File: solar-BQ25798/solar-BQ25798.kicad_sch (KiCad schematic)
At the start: 82 parts, among them J101 Power In, J102 Power OUT, J103 Power OUT, Q101 DMP4013LFGQ-13, Q102 2N7002, U101 HT75xx-1-SOT89, U102 INA219AxDCN

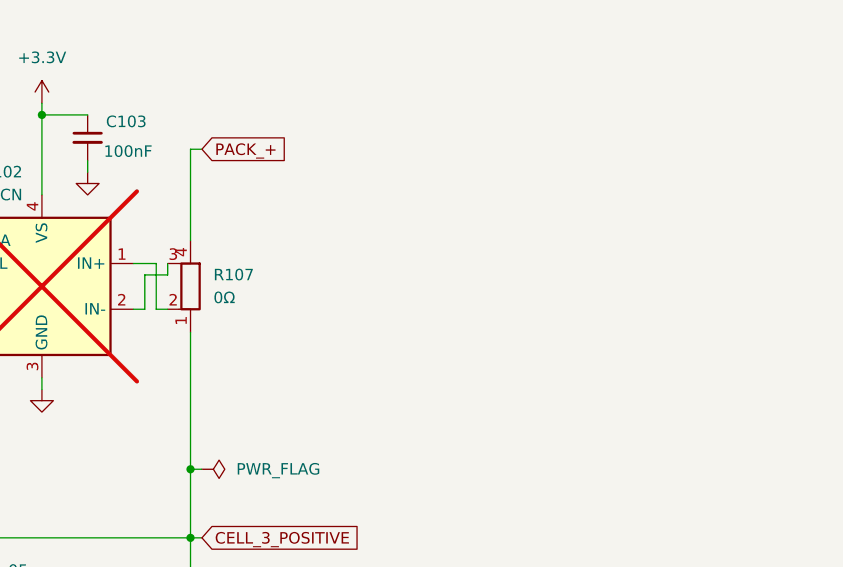
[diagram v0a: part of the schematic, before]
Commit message: Improve optional shunt resistor
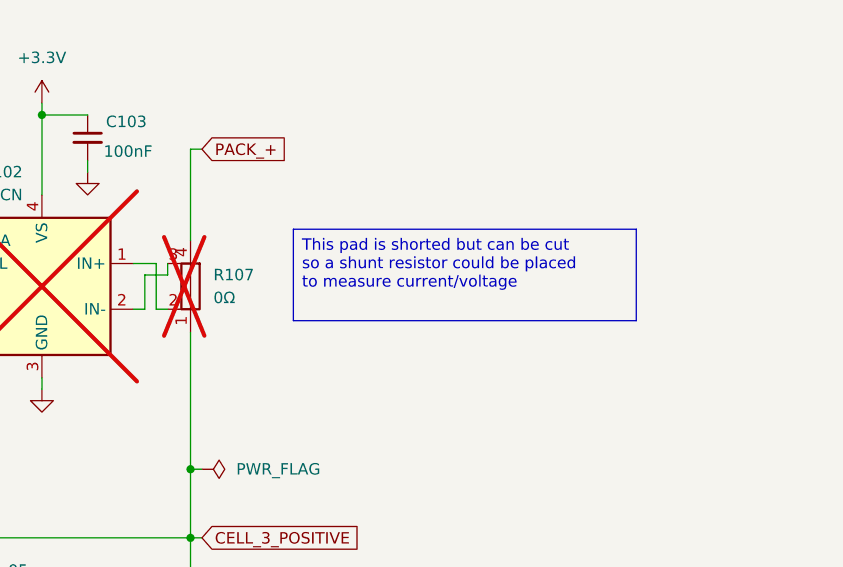
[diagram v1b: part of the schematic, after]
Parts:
- R107: footprint cacophony-library:R_1206_Shunt -> cacophony-library:R_1206_Shunt_Short; symbol Device:R_Shunt -> cacophony-library:R_Shunt_Short; LCSC Part C17888 -> (none); now not fitted; now left out of the parts list
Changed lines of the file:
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@@
 		)
 	)
+	(text_box "This pad is shorted but can be cut so a shunt resistor could be placed to measure current/voltage"
+		(exclude_from_sim no)
+		(at 208.28 163.83 0)
+		(size 38.1 10.16)
+		(margins 0.9525 0.9525 0.9525 0.9525)
+		(stroke
+			(width 0)
+			(type solid)
+		)
+		(fill
+			(type none)
+		)
+		(effects
+			(font
+				(size 1.27 1.27)
+			)
+			(justify left top)
+		)
+	)
 	(junction
 		(at 123.19 224.79)
@@
 	(wire
 		(pts
+			(xy 196.85 175.26) (xy 196.85 190.5)
+		)
+		(stroke
+			(width 0)
+			(type default)
+		)
+	)
+	(wire
+		(pts
 			(xy 121.92 208.28) (xy 123.19 208.28)
 		)
@@
 	(wire
 		(pts
-			(xy 196.85 175.26) (xy 196.85 190.5)
-		)
-		(stroke
-			(width 0)
-			(type default)
-		)
-	)
-	(wire
-		(pts
 			(xy 86.36 279.4) (xy 123.19 279.4)
 		)
@@
 	)
 	(symbol
-		(lib_id "Device:R_Shunt")
+		(lib_id "cacophony-library:R_Shunt_Short")
 		(at 196.85 170.18 180)
 		(unit 1)
 		(body_style 1)
 		(exclude_from_sim no)
-		(in_bom yes)
+		(in_bom no)
 		(on_board yes)
-		(in_pos_files yes)
-		(dnp no)
+		(in_pos_files no)
+		(dnp yes)
 		(property "Reference" "R107"
 			(at 199.39 168.9099 0)
@@
 			)
 		)
-		(property "Footprint" "cacophony-library:R_1206_Shunt"
+		(property "Footprint" "cacophony-library:R_1206_Shunt_Short"
 			(at 198.628 170.18 90)
 			(hide yes)
@@
 			(at 196.85 170.18 0)
 			(hide yes)
-			(show_name no)
-			(do_not_autoplace no)
-			(effects
-				(font
-					(size 1.27 1.27)
-				)
-			)
-		)
-		(property "LCSC Part" "C17888"
-			(at 196.85 170.18 0)
-			(hide yes)

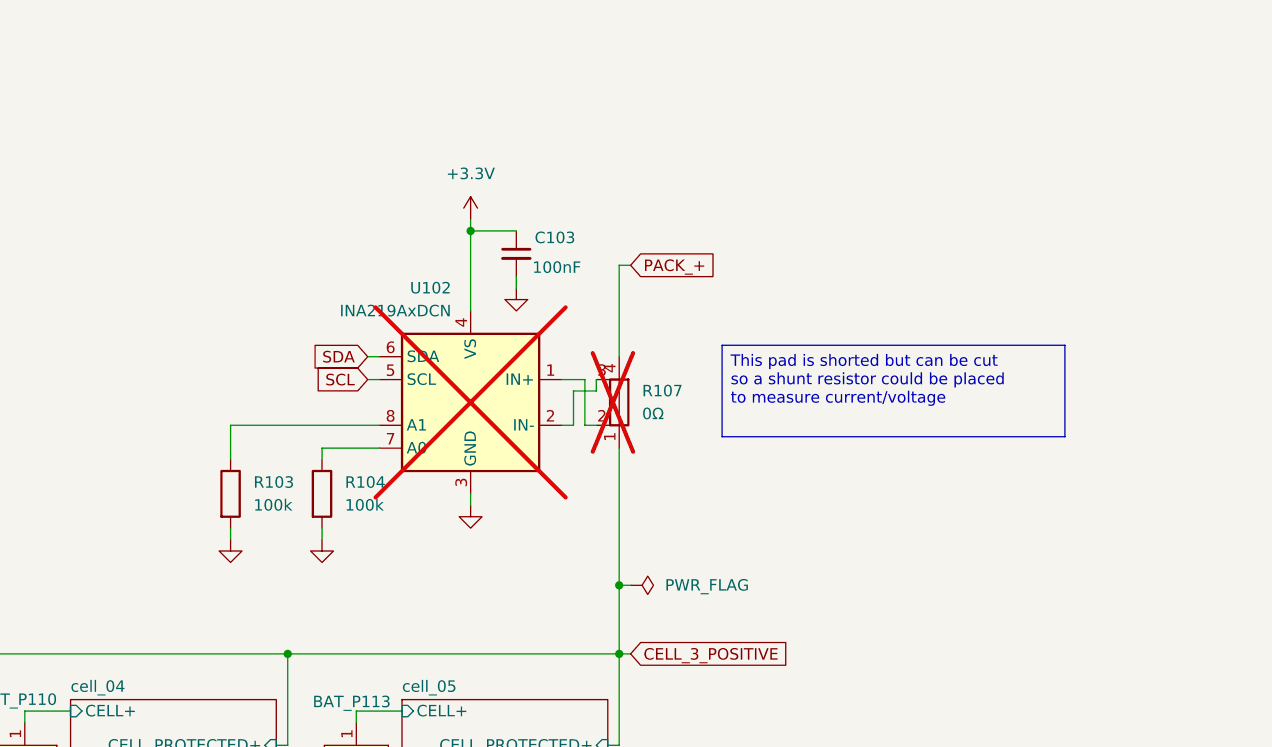
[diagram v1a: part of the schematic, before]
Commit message: Reduce number of different resistor and capacitor values
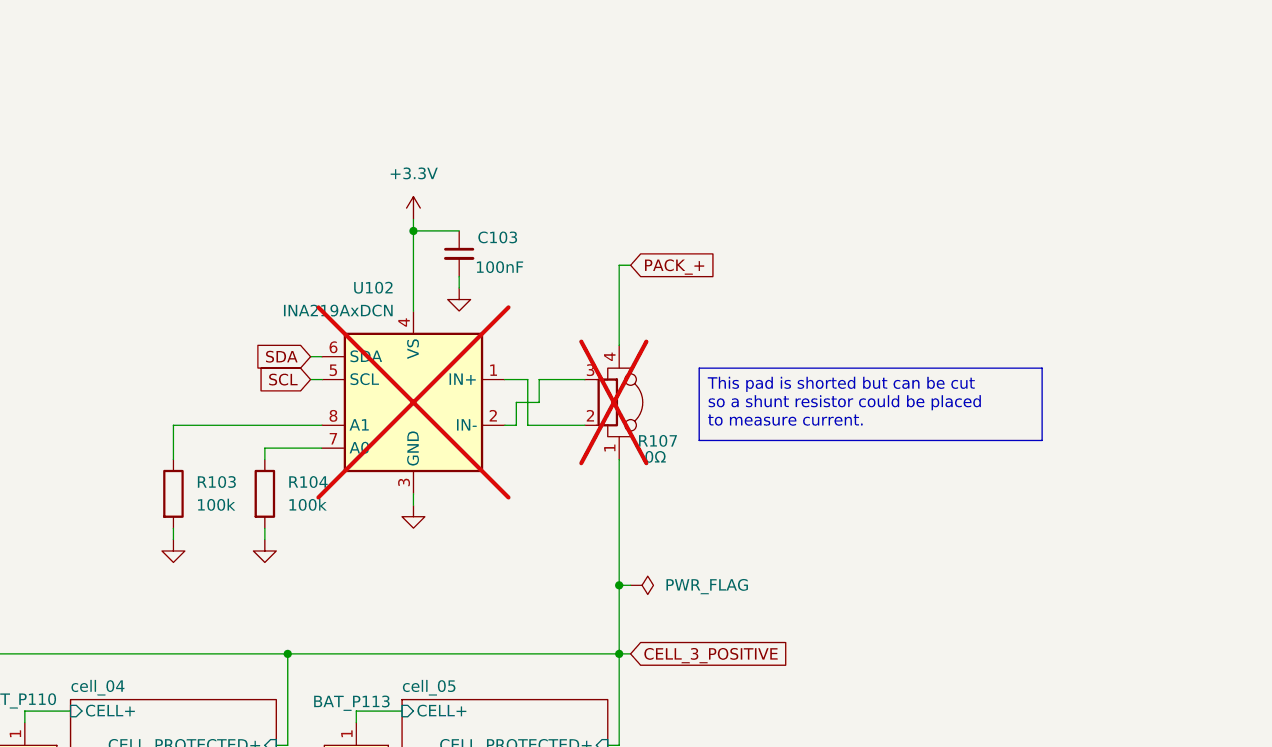
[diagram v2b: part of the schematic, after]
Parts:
- C101, C102: footprint Capacitor_SMD:C_0603_1608Metric -> Capacitor_SMD:C_0402_1005Metric; LCSC Part C15849 -> C52923
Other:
- moved on the sheet: C103, R103, R104, U102

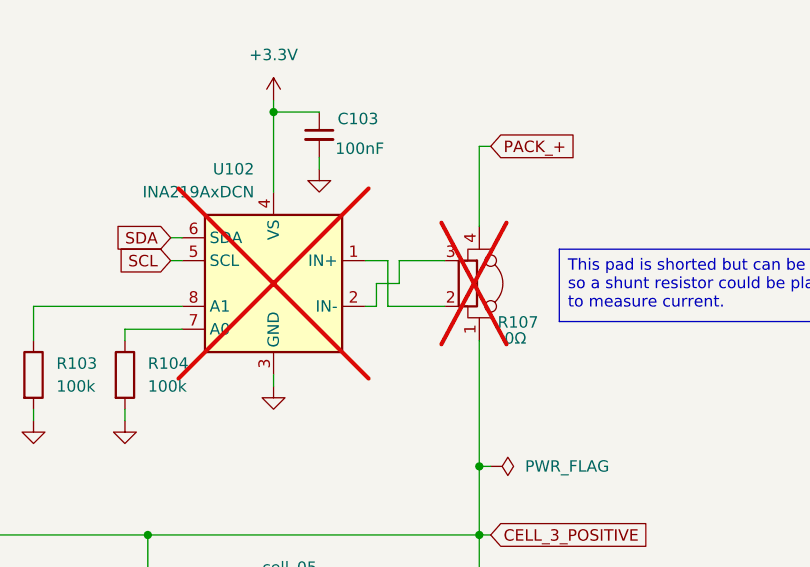
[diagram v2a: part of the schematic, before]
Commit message: Update components LCSC parts
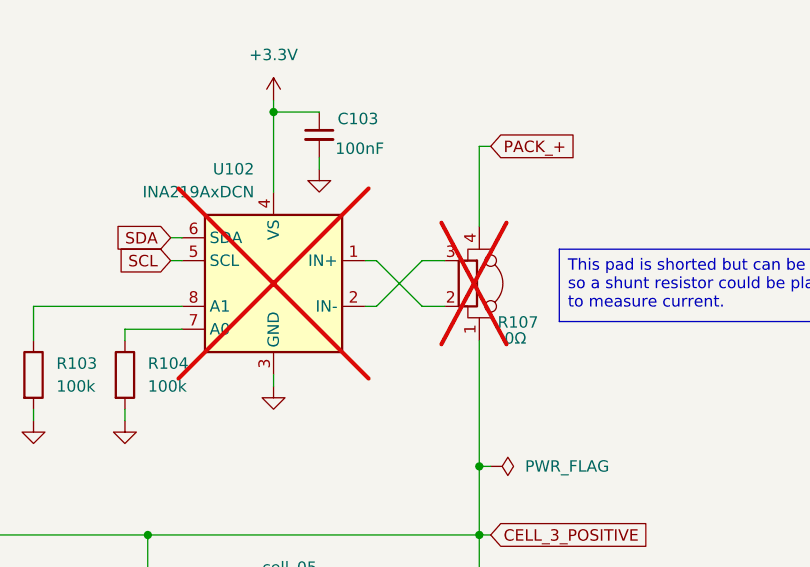
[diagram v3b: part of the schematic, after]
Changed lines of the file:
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@@
+	(wire
+		(pts
+			(xy 190.5 172.72) (xy 193.04 172.72)
+		)
+		(stroke
+			(width 0)
+			(type default)
+		)
+	)
 	(wire
 		(pts
@@
 	(wire
 		(pts
+			(xy 190.5 167.64) (xy 193.04 167.64)
+		)
+		(stroke
+			(width 0)
+			(type default)
+		)
+	)
+	(wire
+		(pts
 			(xy 157.48 175.26) (xy 163.83 175.26)
 		)
@@
 	(wire
 		(pts
-			(xy 185.42 170.18) (xy 187.96 170.18)
-		)
-		(stroke
-			(width 0)
-			(type default)
-		)
-	)
-	(wire
-		(pts
 			(xy 26.67 82.55) (xy 38.1 82.55)
 		)
@@
 	(wire
 		(pts
+			(xy 185.42 167.64) (xy 190.5 172.72)
+		)
+		(stroke
+			(width 0)
+			(type default)
+		)
+	)
+	(wire
+		(pts
 			(xy 49.53 252.73) (xy 86.36 252.73)
 		)
@@
 	(wire
 		(pts
-			(xy 186.69 172.72) (xy 193.04 172.72)
-		)
-		(stroke
-			(width 0)
-			(type default)
-		)
-	)
-	(wire
-		(pts
-			(xy 186.69 167.64) (xy 186.69 172.72)
-		)
-		(stroke
-			(width 0)
-			(type default)
-		)
-	)
-	(wire
-		(pts
 			(xy 48.26 208.28) (xy 49.53 208.28)
 		)
@@
 	(wire
 		(pts
-			(xy 187.96 167.64) (xy 193.04 167.64)
-		)
-		(stroke
-			(width 0)
-			(type default)
-		)
-	)
-	(wire
-		(pts
 			(xy 48.26 262.89) (xy 49.53 262.89)
 		)
@@
 	(wire
 		(pts
-			(xy 187.96 167.64) (xy 187.96 170.18)
-		)
-		(stroke
-			(width 0)
-			(type default)
-		)
-	)
-	(wire
-		(pts
 			(xy 38.1 81.28) (xy 38.1 82.55)
 		)
@@
 	(wire
 		(pts
-			(xy 185.42 172.72) (xy 185.42 170.18)
-		)
-		(stroke
-			(width 0)
-			(type default)
-		)
-	)
-	(wire
-		(pts
 			(xy 195.58 262.89) (xy 196.85 262.89)
 		)
@@
 	(wire
 		(pts
-			(xy 184.15 167.64) (xy 186.69 167.64)
-		)
-		(stroke
-			(width 0)
-			(type default)
-		)
-	)
-	(wire
-		(pts
 			(xy 189.23 26.67) (xy 193.04 26.67)
 		)
@@
 	(wire
 		(pts
+			(xy 184.15 167.64) (xy 185.42 167.64)
+		)
+		(stroke
+			(width 0)
+			(type default)
+		)
+	)
+	(wire
+		(pts
 			(xy 167.64 205.74) (xy 167.64 204.47)
 		)
@@
 		)
 		(stroke
+			(width 0)
+			(type default)
+		)
+	)
+	(wire
+		(pts
+			(xy 185.42 172.72) (xy 190.5 167.64)
+		)
+		(stroke

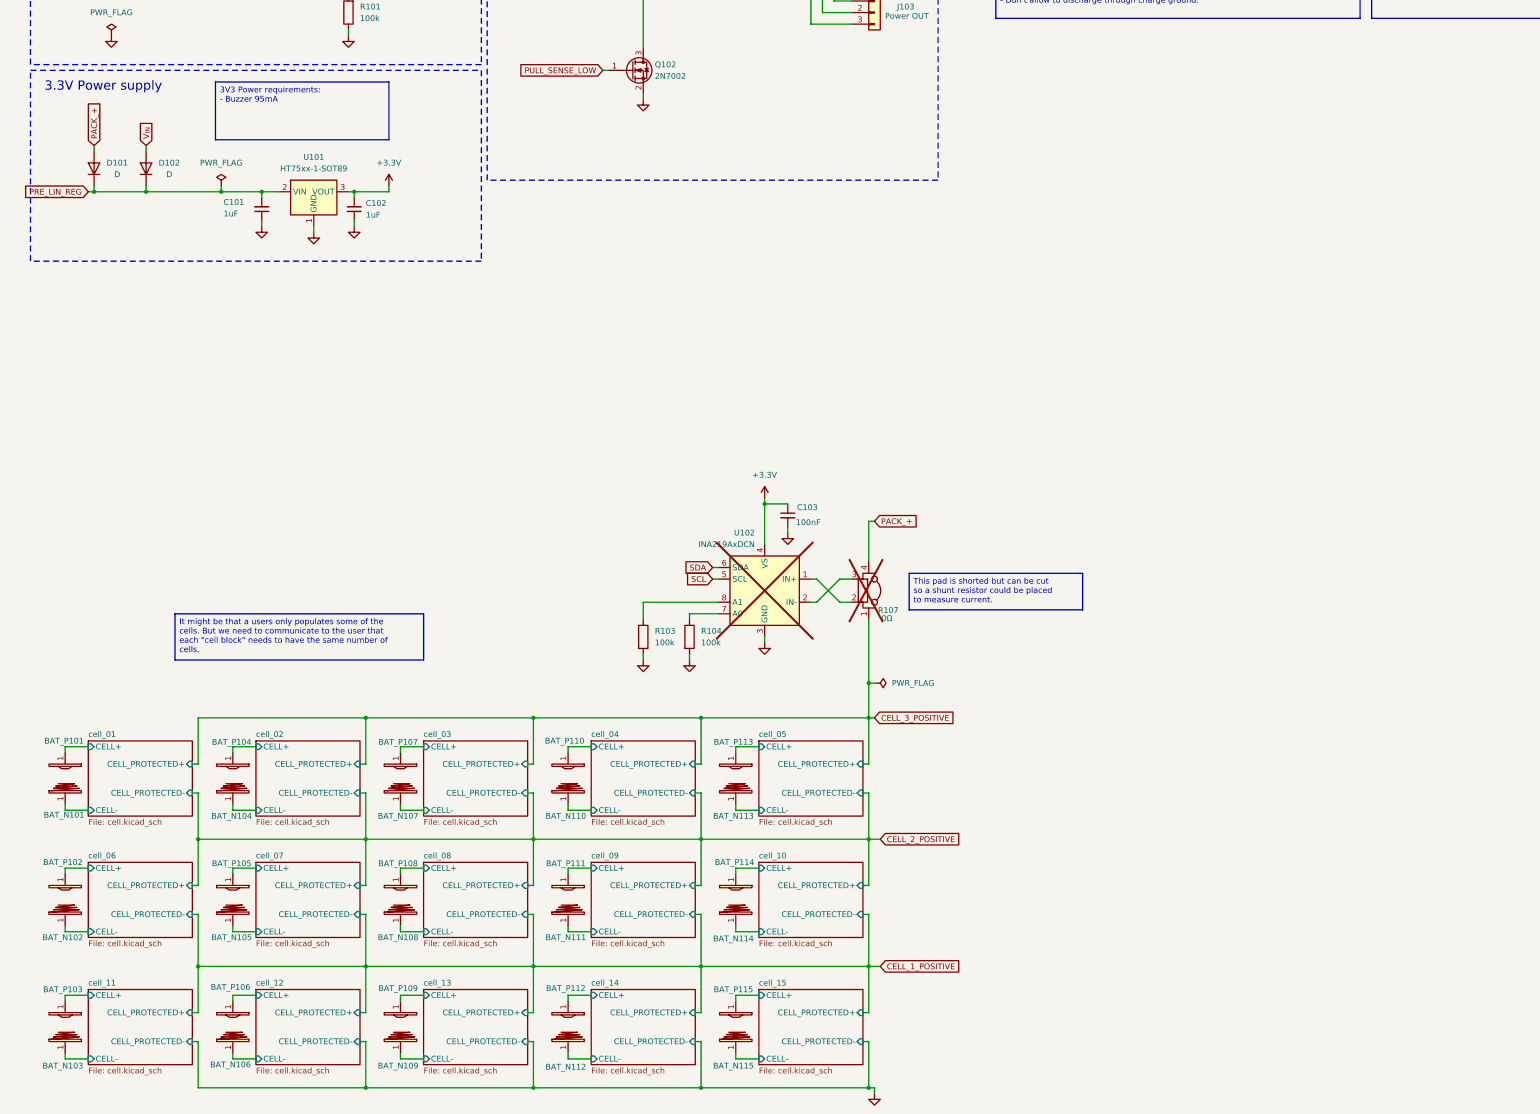
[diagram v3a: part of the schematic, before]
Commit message: Add heating element
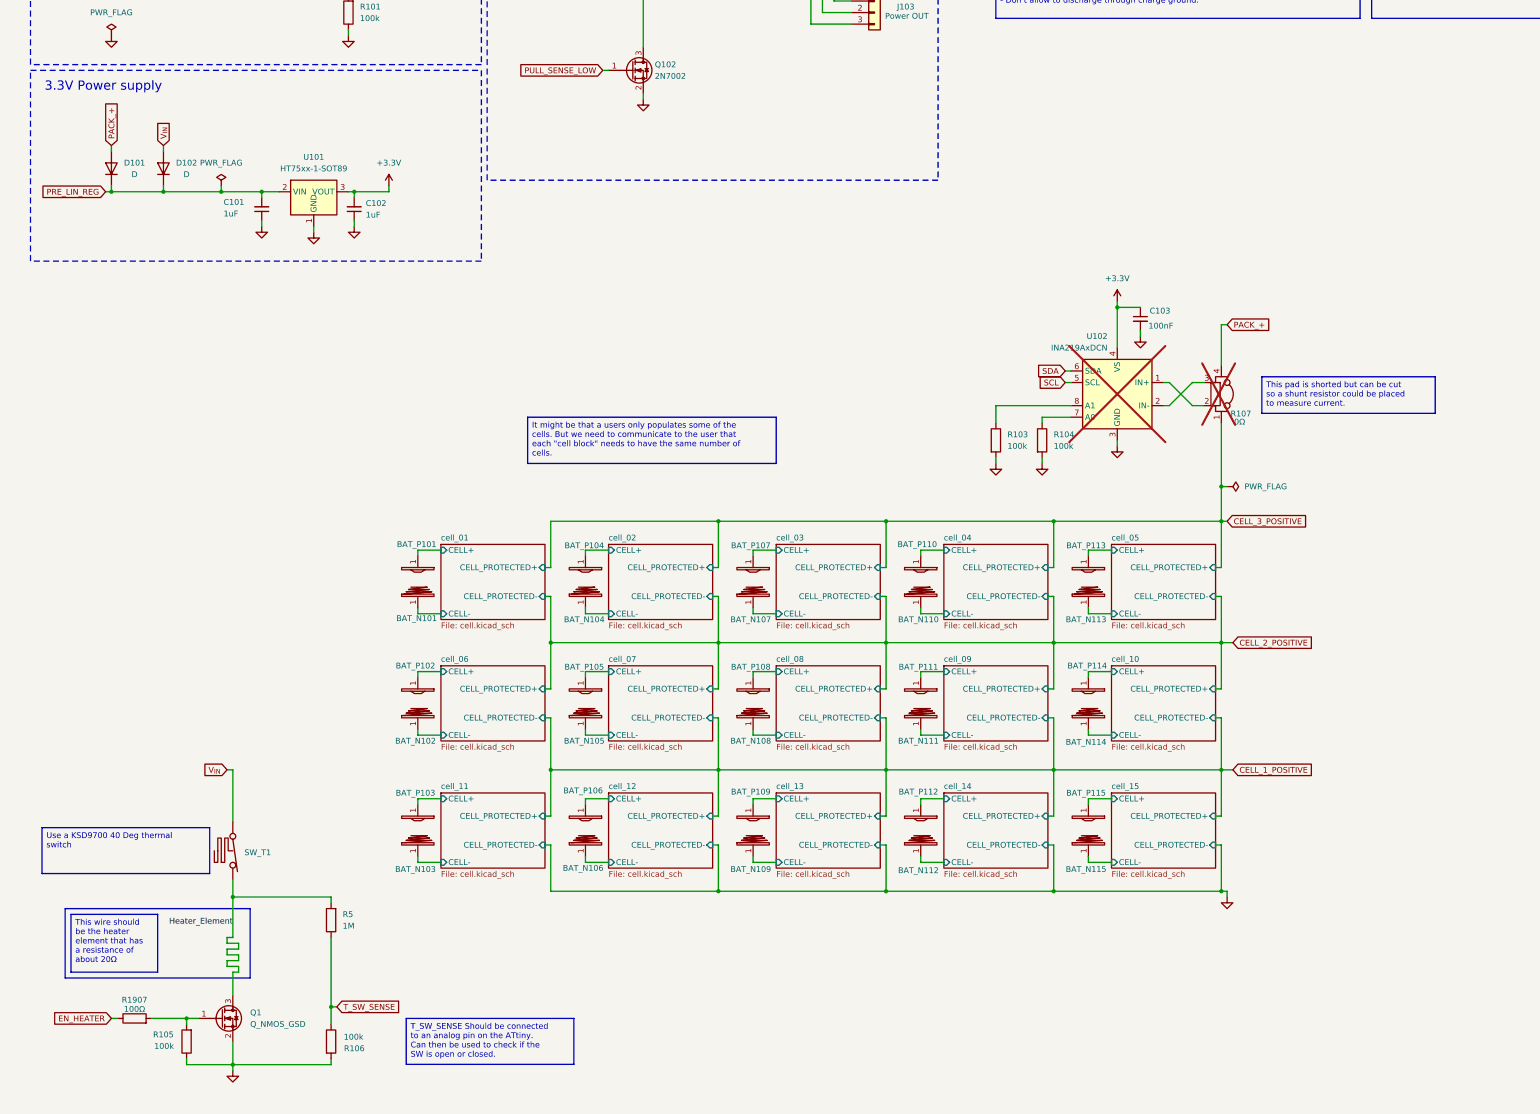
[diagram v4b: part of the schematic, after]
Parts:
- added Q1: Q_NMOS_GSD, Package_TO_SOT_SMD:SOT-23, symbol Transistor_FET:Q_NMOS_GSD
- added R105, R106: 100k, Resistor_SMD:R_0402_1005Metric, symbol Device:R
- added R1907: 100Ω, Resistor_SMD:R_0402_1005Metric, symbol Device:R
- added R5: 1M, Resistor_SMD:R_0402_1005Metric, symbol Device:R
- added SW_T1: (no value), cacophony-library:KSD9700, symbol cacophony-library:Thermostat_Switch
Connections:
- net GND: now also Q1.2 (S), R105.1, R106.2
- net V_{IN}: now also SW_T1.1
- new net: Q1.1 (G), R105.2, R1907.2
- new net EN_HEATER: R1907.1
- new net Heater_Element: Q1.3 (D), R5.2, SW_T1.2
- new net T_SW_SENSE: R106.1, R5.1
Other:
- moved on the sheet: BAT_N101, BAT_N102, BAT_N103, BAT_N104, BAT_N105, BAT_N106, BAT_N107, BAT_N108, BAT_N109, BAT_N110, BAT_N111, BAT_N112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

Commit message: Update buzzer and 3D files
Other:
- moved on the sheet: C101, C102, D101, D102, U101
